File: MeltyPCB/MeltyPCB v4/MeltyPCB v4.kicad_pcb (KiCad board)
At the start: 2 copper layers, 65.5 x 68.9 mm, 23 parts, among them U0 Teensy 4.0, U1 XIAO_ESP32_S3

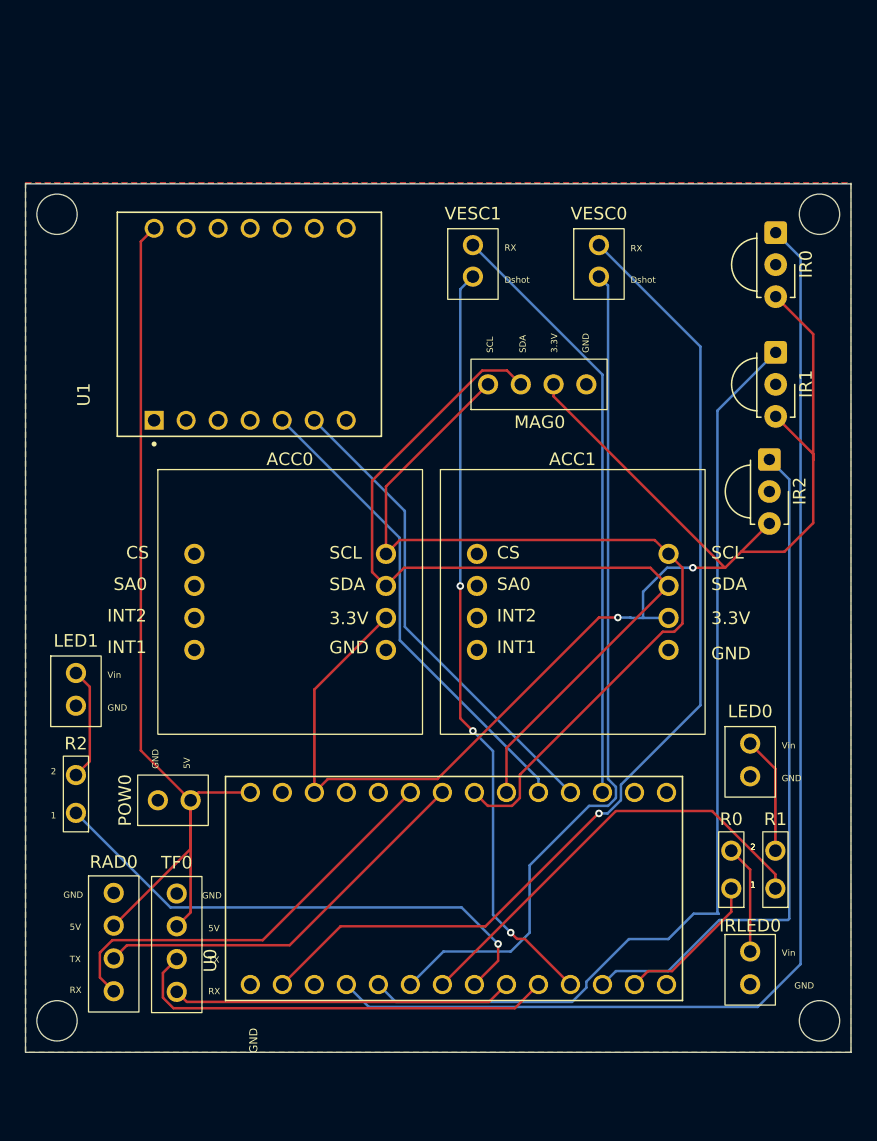
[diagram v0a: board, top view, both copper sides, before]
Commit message: Updated MeltyPCB v4 + Kicad Libraries
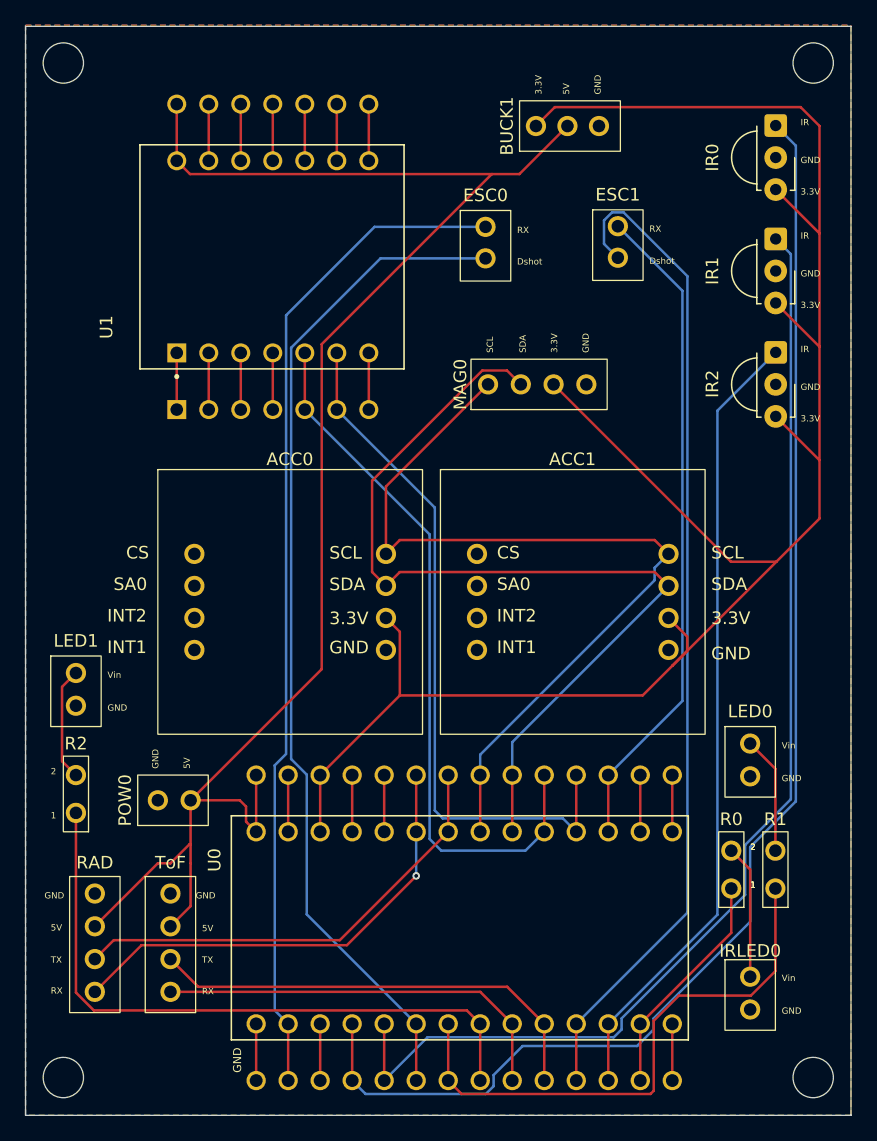
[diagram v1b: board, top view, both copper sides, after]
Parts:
- added BUCK1: ~, MeltyPCB:Buck Converter, F.Cu at (93.7, 42.5)
- U0: footprint Teensy_4.0:Teensy 4.0 (Simplified) -> Teensy_4.0:Teensy 4.0 (Simplified) (Extra Holes)
- U1: footprint XIAO_ESP32_S3:MODULE_XIAO_ESP32_S3 -> XIAO_ESP32_S3:XIAO_ESP32_S3 (Extra Holes)
- moved ? 12.0 mm to (117.5, 37.5)
- moved ? 12.0 mm to (58.0, 37.5)
- moved ESC1 11.6 mm to (102.0, 48.5)
- moved ESC0 9.12 mm to (91.5, 48.5)
- moved IR1 9.00 mm to (114.5, 51.5)
- moved IR2 8.51 mm to (114.5, 60.5)
- moved IR0 8.50 mm to (114.5, 42.5)
- moved U1 5.65 mm to (74.6, 52.9)
- moved ? 4.53 mm to (58.0, 118.0)
- moved ? 4.53 mm to (117.5, 118.0)
- moved U0 3.15 mm to (89.8, 106.1)
- moved IRLED0 2.00 mm to (112.5, 108.0)
- moved RAD 1.50 mm to (60.5, 101.5)
- moved ToF 0.50 mm to (66.5, 101.5)
- renumbered VESC0 to ESC0, VESC1 to ESC1, RAD0 to RAD, TF0 to ToF
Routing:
- net +5V: track 75.4 -> 129.5 mm
- net +3.3V: track 115.2 -> 157.2 mm, vias 2 -> 0
- net /SDA1: track 38.0 -> 57.3 mm
- net /Dshot1: track 60.6 -> 79.9 mm, vias 3 -> 0
- net /SCL1: track 38.0 -> 56.0 mm
- net /IR1: track 77.2 -> 93.8 mm
- net GND: track 0.00 -> 13.5 mm
- net /Dshot0: track 67.5 -> 80.6 mm
- net /IR0: track 97.0 -> 108.6 mm
- net /LED1: track 50.8 -> 60.9 mm, vias 1 -> 0
- net /LED0: track 44.7 -> 54.1 mm
- net /IR2: track 54.1 -> 63.3 mm
- net /IRLED: track 20.5 -> 28.9 mm
- net /RX2: track 27.1 -> 32.7 mm
- net /TX5: track 31.5 -> 36.7 mm
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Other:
- board size 65.5 x 68.9 mm -> 65.5 x 86.4 mm
- board text added: "3.3V"
- board text added: "GND"
- board text added: "IR"
